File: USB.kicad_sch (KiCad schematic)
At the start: 14 parts, among them J1 USB_B_Micro, Q1 BC847, Q2 BC847, U2 CP2102N-Axx-xQFN28

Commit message: Fixed PCB errors
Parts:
- removed Q2: BC847, Package_TO_SOT_SMD:SOT-363_SC-70-6, symbol Transistor_BJT:BC847
- added Q3: BC847, Package_TO_SOT_SMD:SOT-23, symbol Transistor_BJT:BC847
- Q1: footprint Package_TO_SOT_SMD:SOT-363_SC-70-6 -> Package_TO_SOT_SMD:SOT-23
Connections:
- net DTR: now also Q3.2 (E)
- net IO0: now also Q3.3 (C)
- net at R6.2: now also Q3.1 (B)
- no-connect marks 1 -> 17
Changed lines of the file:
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@@
+	)
+	(no_connect
+		(at 106.68 140.97)
+	)
+	(no_connect
+		(at 106.68 179.07)
+	)
+	(no_connect
+		(at 106.68 158.75)
+	)
+	(no_connect
+		(at 106.68 166.37)
+	)
+	(no_connect
+		(at 106.68 168.91)
+	)
+	(no_connect
+		(at 106.68 176.53)
+	)
+	(no_connect
+		(at 106.68 135.89)
+	)
+	(no_connect
+		(at 106.68 181.61)
+	)
+	(no_connect
+		(at 106.68 163.83)
 	)
 	(no_connect
 		(at 64.77 55.88)
+	)
+	(no_connect
+		(at 106.68 151.13)
+	)
+	(no_connect
+		(at 106.68 148.59)
+	)
+	(no_connect
+		(at 106.68 133.35)
+	)
+	(no_connect
+		(at 106.68 143.51)
+	)
+	(no_connect
+		(at 106.68 161.29)
+	)
+	(no_connect
+		(at 106.68 171.45)
+	)
+	(no_connect
+		(at 106.68 156.21)
 	)
 	(wire
@@
 	(symbol
 		(lib_id "Transistor_BJT:BC847")
-		(at 219.71 44.45 0)
+		(at 219.71 62.23 0)
 		(unit 1)
 		(exclude_from_sim no)
@@
 		(dnp no)
 		(fields_autoplaced yes)
-		(property "Reference" "Q1"
-			(at 224.79 43.1799 0)
+		(property "Reference" "Q3"
+			(at 224.79 60.9599 0)
 			(effects
 				(font
@@
 		)
 		(property "Value" "BC847"
-			(at 224.79 45.7199 0)
+			(at 224.79 63.4999 0)
 			(effects
 				(font
@@
 			)
 		)
-		(property "Footprint" "Package_TO_SOT_SMD:SOT-363_SC-70-6"
-			(at 224.79 46.355 0)
+		(property "Footprint" "Package_TO_SOT_SMD:SOT-23"
+			(at 224.79 64.135 0)
 			(effects
 				(font
@@
 		)
 		(property "Datasheet" "http://www.infineon.com/dgdl/Infineon-BC847SERIES_BC848SERIES_BC849SERIES_BC850SERIES-DS-v01_01-en.pdf?fileId=db3a304314dca389011541d4630a1657"
-			(at 219.71 44.45 0)
+			(at 219.71 62.23 0)
 			(effects
 				(font
@@
 		)
 		(property "Description" "0.1A Ic, 45V Vce, NPN Transistor, SOT-23"
-			(at 219.71 44.45 0)
+			(at 219.71 62.23 0)
 			(effects
 				(font
@@
 		(pin "2"
 		)
+		(pin "1"
+		)
 		(pin "3"
-		)
-		(pin "1"
 		)
 		(instances
 			(project ""
 				(path "/32966cbd-337b-4fa7-b66f-bfe62b1c18c3/450de07c-431b-41c3-b4dc-3003fe77996d"
-					(reference "Q1")
+					(reference "Q3")
 					(unit 1)
 				)
@@
 	(symbol
 		(lib_id "Transistor_BJT:BC847")
-		(at 219.71 62.23 0)
+		(at 219.71 44.45 0)
 		(unit 1)
 		(exclude_from_sim no)
@@
 		(dnp no)
 		(fields_autoplaced yes)
-		(property "Reference" "Q2"
-			(at 224.79 60.9599 0)
+		(property "Reference" "Q1"
+			(at 224.79 43.1799 0)
 			(effects
 				(font
@@
 		)
 		(property "Value" "BC847"
-			(at 224.79 63.4999 0)
+			(at 224.79 45.7199 0)
 			(effects
 				(font
@@
 			)
 		)
-		(property "Footprint" "Package_TO_SOT_SMD:SOT-363_SC-70-6"
-			(at 224.79 64.135 0)
+		(property "Footprint" "Package_TO_SOT_SMD:SOT-23"
+			(at 224.79 46.355 0)
 			(effects
 				(font
@@
 		)
 		(property "Datasheet" "http://www.infineon.com/dgdl/Infineon-BC847SERIES_BC848SERIES_BC849SERIES_BC850SERIES-DS-v01_01-en.pdf?fileId=db3a304314dca389011541d4630a1657"
-			(at 219.71 62.23 0)
+			(at 219.71 44.45 0)
 			(effects
 				(font
@@
 		)
 		(property "Description" "0.1A Ic, 45V Vce, NPN Transistor, SOT-23"
-			(at 219.71 62.23 0)
+			(at 219.71 44.45 0)
 			(effects
 				(font
@@
 		(pin "2"
 		)
+		(pin "1"
+		)
 		(pin "3"
-		)
-		(pin "1"
 		)
 		(instances
 			(project "Airboat"
 				(path "/32966cbd-337b-4fa7-b66f-bfe62b1c18c3/450de07c-431b-41c3-b4dc-3003fe77996d"
-					(reference "Q2")
+					(reference "Q1")
 					(unit 1)
 				)

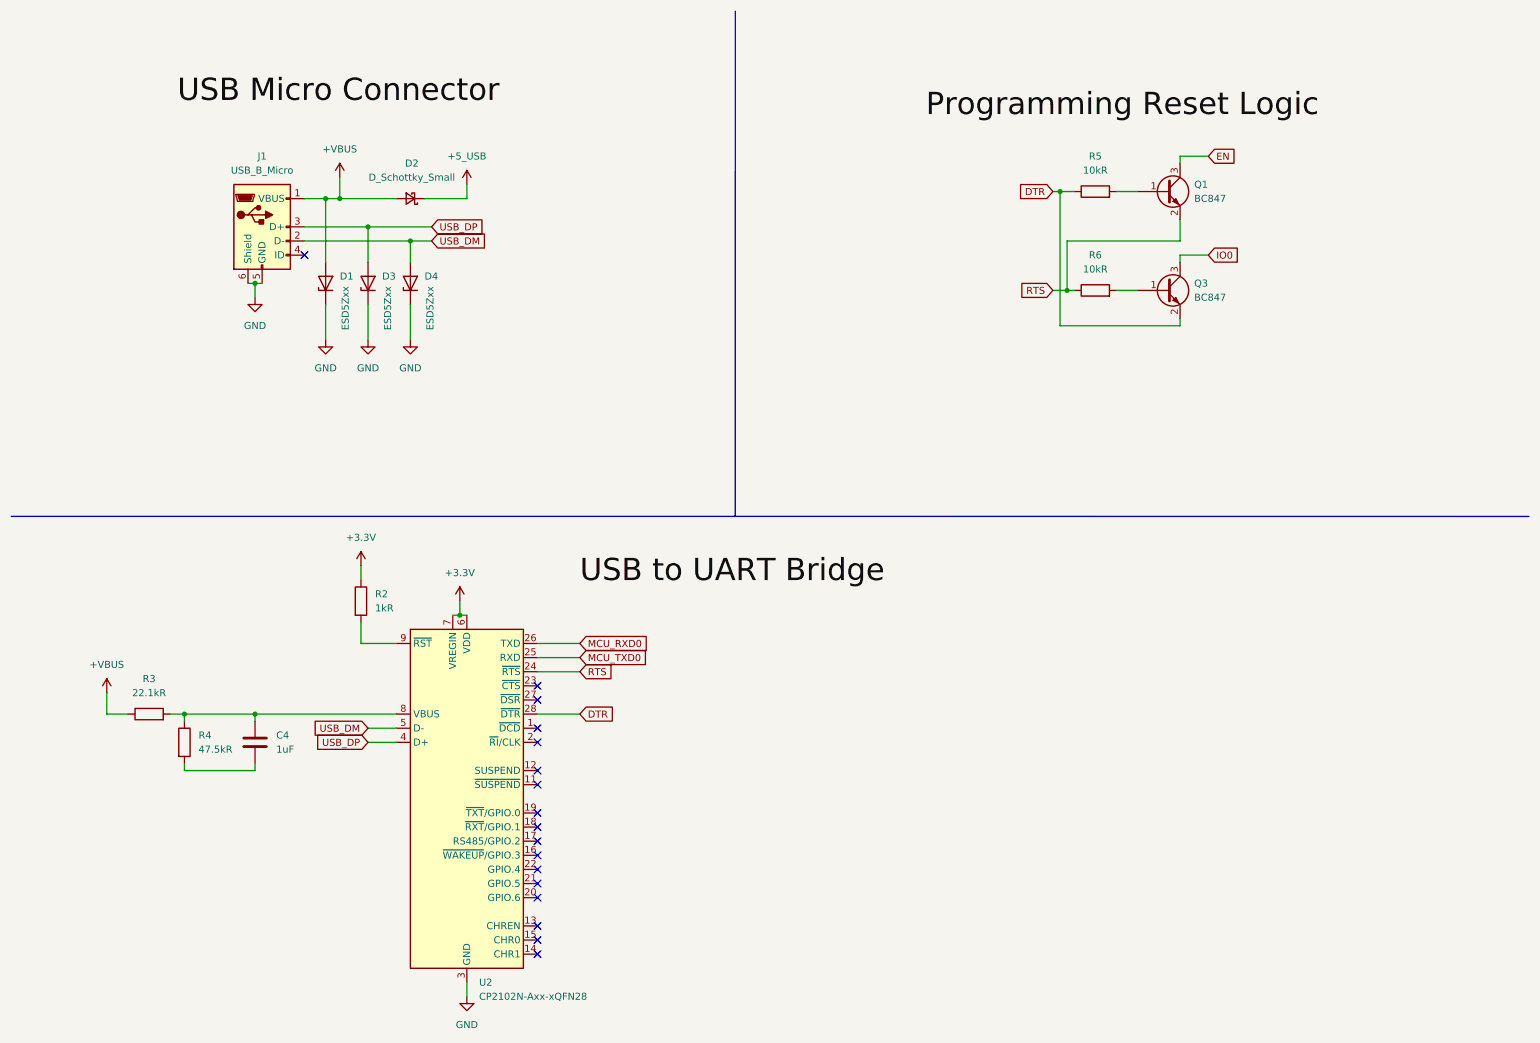
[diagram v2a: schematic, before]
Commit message: Placed all components on PCB
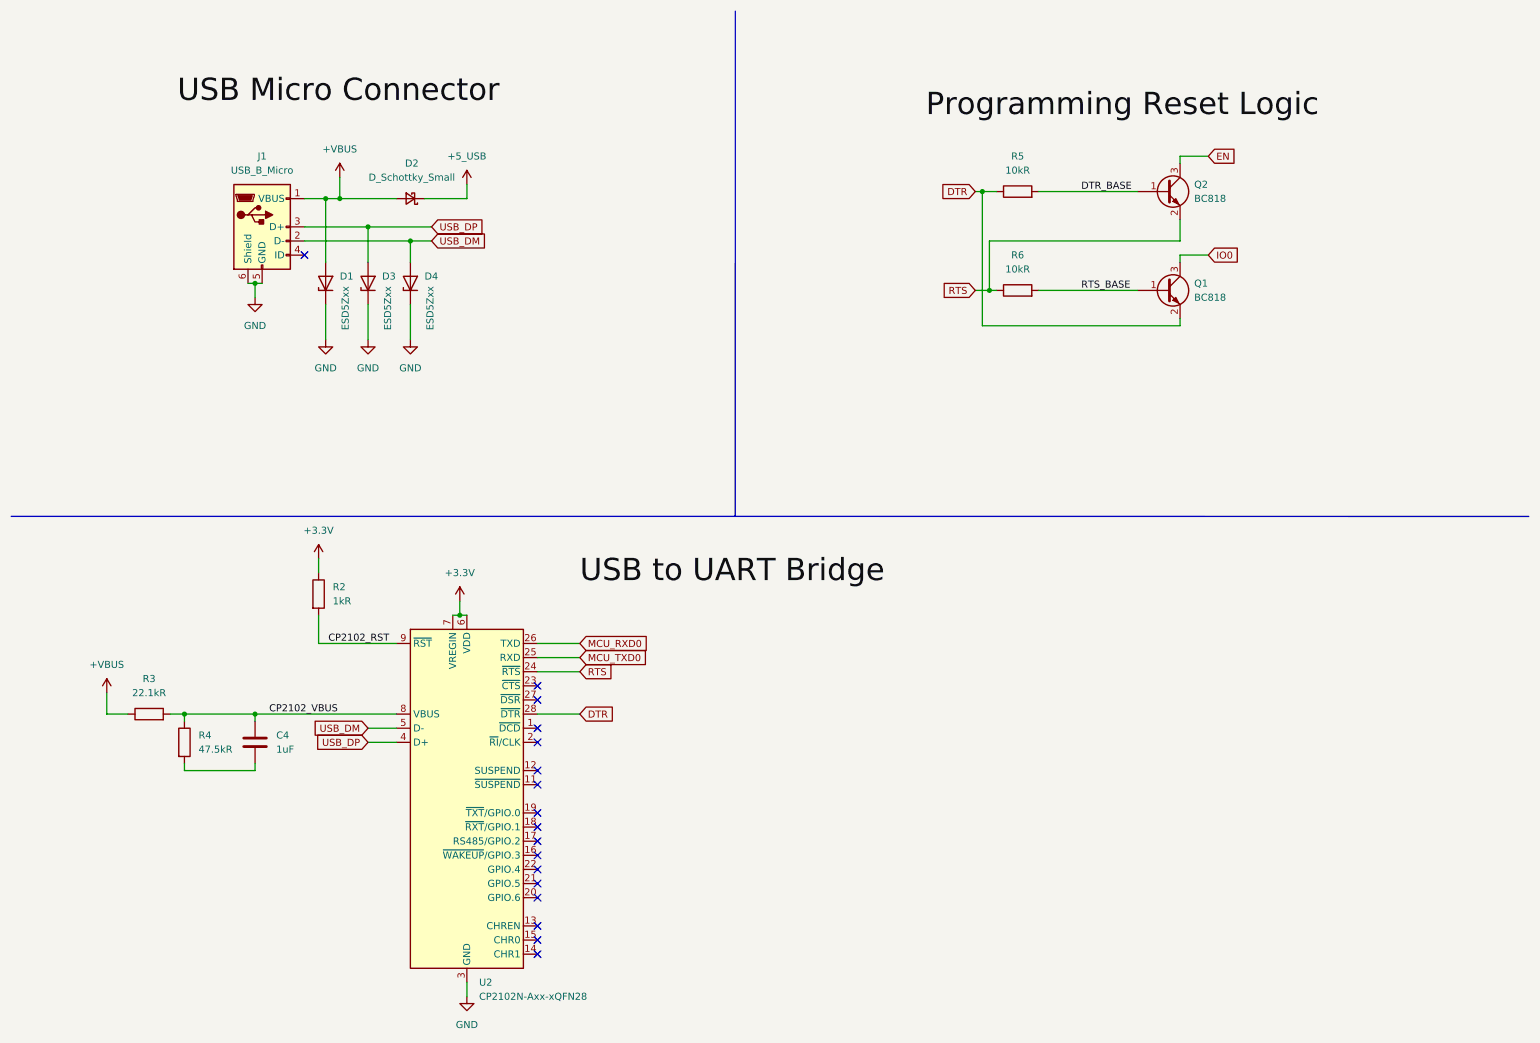
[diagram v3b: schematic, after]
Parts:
- removed Q1, Q3: BC847, Package_TO_SOT_SMD:SOT-23, symbol Transistor_BJT:BC847
- added Q1, Q2: BC818, Package_TO_SOT_SMD:SOT-23, symbol Transistor_BJT:BC818
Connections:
- net DTR: now also Q1.2 (E)
- net EN: now also Q2.3 (C)
- net IO0: now also Q1.3 (C)
- net RTS: now also Q2.2 (E)
- net CP2102_VBUS: now reaches C4.1, R3.2, R4.1, U2.8 (VBUS)
- net CP2102_RST: now reaches R2.2, U2.9 (~{RST})
- net RTS_BASE: now reaches R6.2
- net RTS_BASE: now also Q1.1 (B)
- net DTR_BASE: now reaches R5.2
- net DTR_BASE: now also Q2.1 (B)
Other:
- moved on the sheet: R2, R5, R6

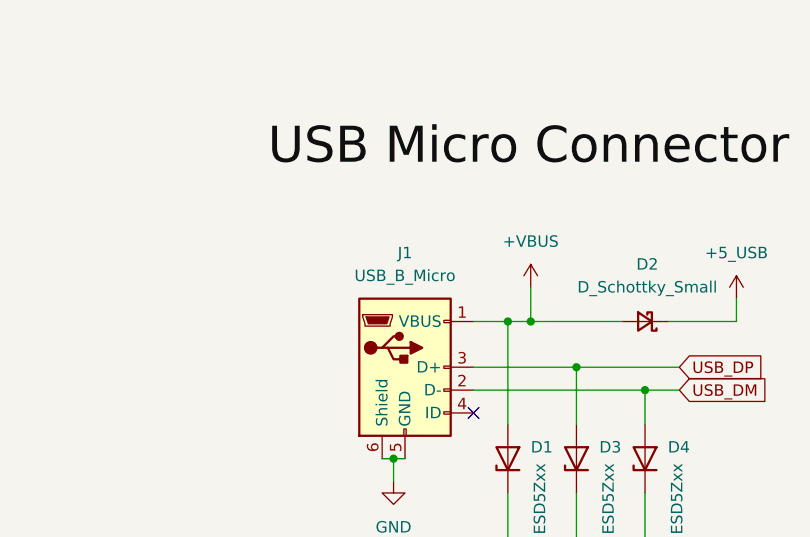
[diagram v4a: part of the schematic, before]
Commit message: Updated PCB to be smaller and support stepper
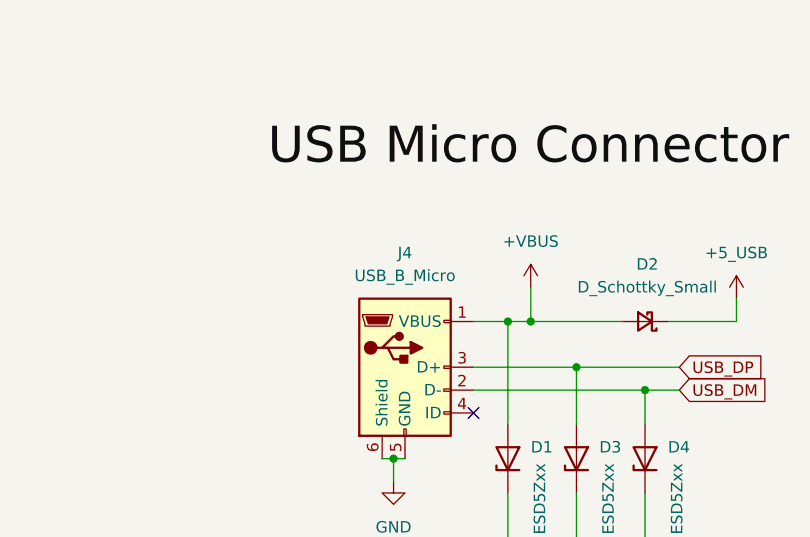
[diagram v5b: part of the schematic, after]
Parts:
- removed J1: USB_B_Micro, Connector_USB:USB_Micro-AB_Molex_47590-0001, symbol Connector:USB_B_Micro
- added J4: USB_B_Micro, Connector_USB:USB_Micro-B_GCT_USB3076-30-A, symbol Connector:USB_B_Micro
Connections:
- net +VBUS: now also J4.1 (VBUS)
- net GND: now also J4.5 (GND), J4.6 (Shield)
- net USB_DM: now also J4.2 (D-)
- net USB_DP: now also J4.3 (D+)
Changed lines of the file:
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@@
-	)
-	(symbol
-		(lib_id "Connector:USB_B_Micro")
-		(at 57.15 50.8 0)
-		(unit 1)
-		(exclude_from_sim no)
-		(in_bom yes)
-		(on_board yes)
-		(dnp no)
-		(fields_autoplaced yes)
-		(property "Reference" "J1"
-			(at 57.15 38.1 0)
-			(effects
-				(font
-					(size 1.27 1.27)
-				)
-			)
-		)
-		(property "Value" "USB_B_Micro"
-			(at 57.15 40.64 0)
-			(effects
-				(font
-					(size 1.27 1.27)
-				)
-			)
-		)
-		(property "Footprint" "Connector_USB:USB_Micro-AB_Molex_47590-0001"
-			(at 60.96 52.07 0)
-			(effects
-				(font
-					(size 1.27 1.27)
-				)
-				(hide yes)
-			)
-		)
-		(property "Datasheet" "~"
-			(at 60.96 52.07 0)
-			(effects
-				(font
-					(size 1.27 1.27)
-				)
-				(hide yes)
-			)
-		)
-		(property "Description" "USB Micro Type B connector"
-			(at 57.15 50.8 0)
-			(effects
-				(font
-					(size 1.27 1.27)
-				)
-				(hide yes)
-			)
-		)
-		(pin "6"
-		)
-		(pin "2"
-		)
-		(pin "1"
-		)
-		(pin "4"
-		)
-		(pin "5"
-		)
-		(pin "3"
-		)
-		(instances
-			(project "Airboat"
-				(path "/32966cbd-337b-4fa7-b66f-bfe62b1c18c3/450de07c-431b-41c3-b4dc-3003fe77996d"
-					(reference "J1")
-					(unit 1)
-				)
-			)
-		)
 	)
 	(symbol
@@
 					(unit 1)
 				)
+			)
+		)
+	)
+	(symbol
+		(lib_id "Connector:USB_B_Micro")
+		(at 57.15 50.8 0)
+		(unit 1)
+		(exclude_from_sim no)
+		(in_bom yes)
+		(on_board yes)
+		(dnp no)
+		(fields_autoplaced yes)
+		(property "Reference" "J4"
+			(at 57.15 38.1 0)
+			(effects
+				(font
+					(size 1.27 1.27)
+				)
+			)
+		)
+		(property "Value" "USB_B_Micro"
+			(at 57.15 40.64 0)
+			(effects
+				(font
+					(size 1.27 1.27)
+				)
+			)
+		)
+		(property "Footprint" "Connector_USB:USB_Micro-B_GCT_USB3076-30-A"
+			(at 60.96 52.07 0)
+			(effects
+				(font
+					(size 1.27 1.27)
+				)
+				(hide yes)
+			)
+		)
+		(property "Datasheet" "~"
+			(at 60.96 52.07 0)
+			(effects
+				(font
+					(size 1.27 1.27)
+				)
+				(hide yes)
+			)
+		)
+		(property "Description" "USB Micro Type B connector"
+			(at 57.15 50.8 0)
+			(effects
+				(font
+					(size 1.27 1.27)
+				)
+				(hide yes)
+			)
+		)
+		(pin "1"
+		)
+		(pin "2"
+		)
+		(pin "5"
+		)
+		(pin "4"
+		)
+		(pin "3"
+		)
+		(pin "6"
+		)
+		(instances
+			(project ""
+				(path "/32966cbd-337b-4fa7-b66f-bfe62b1c18c3/450de07c-431b-41c3-b4dc-3003fe77996d"
+					(reference "J4")
+					(unit 1)
+				)

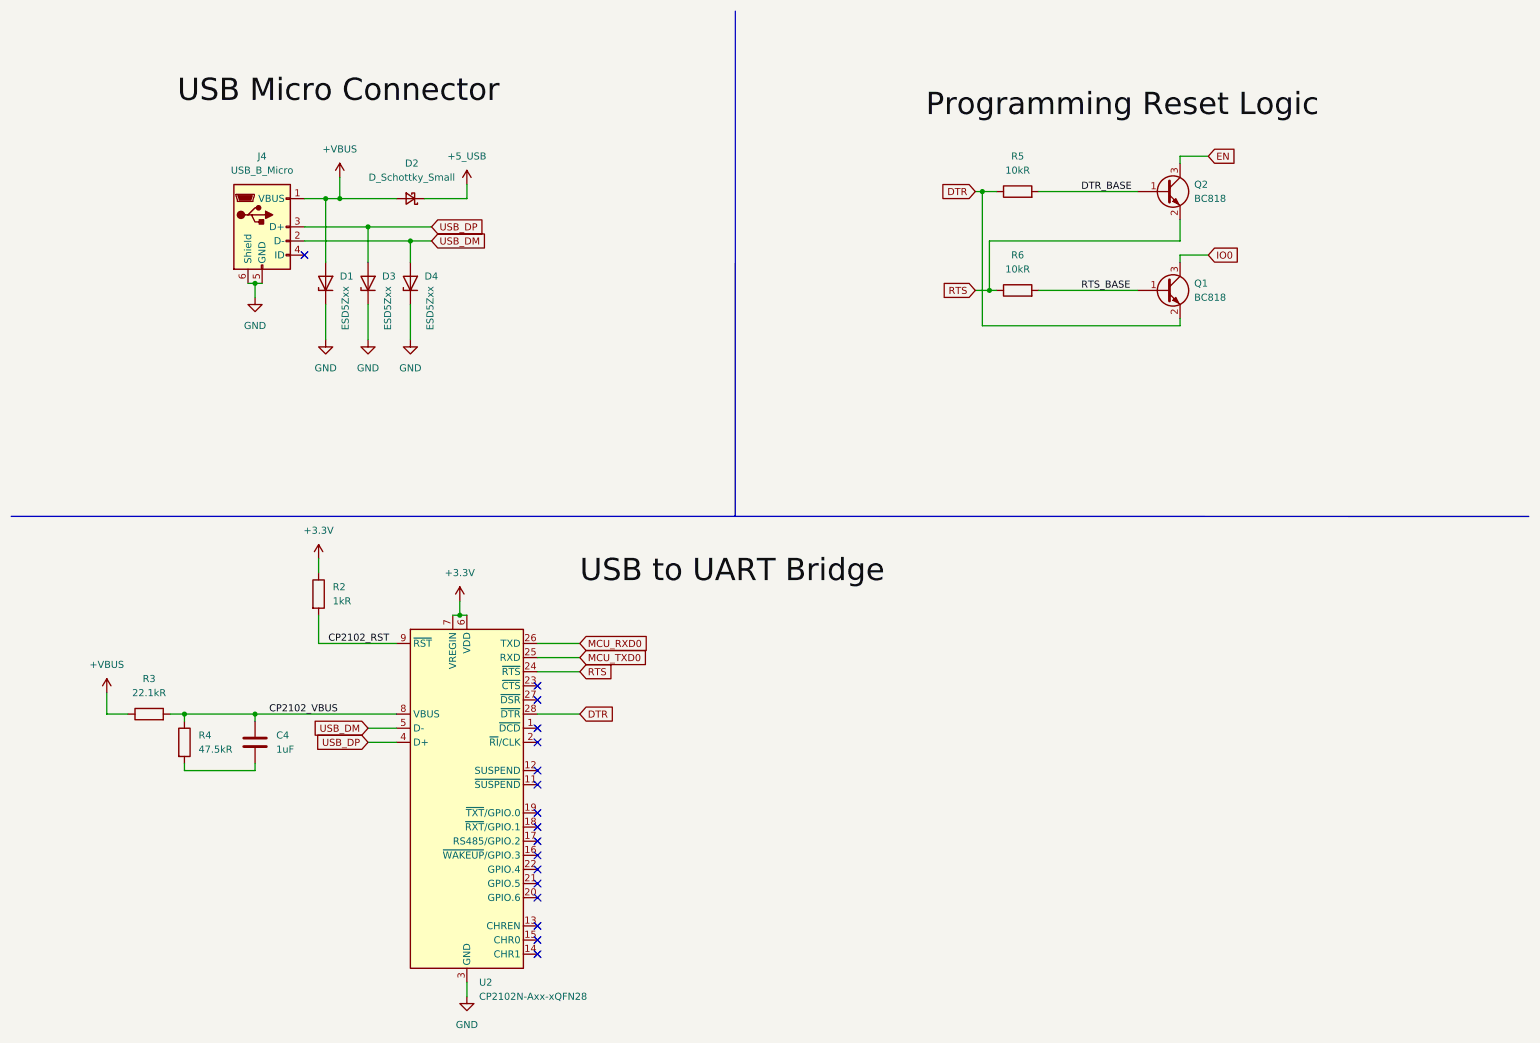
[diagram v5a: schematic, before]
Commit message: Updated to use boost converters
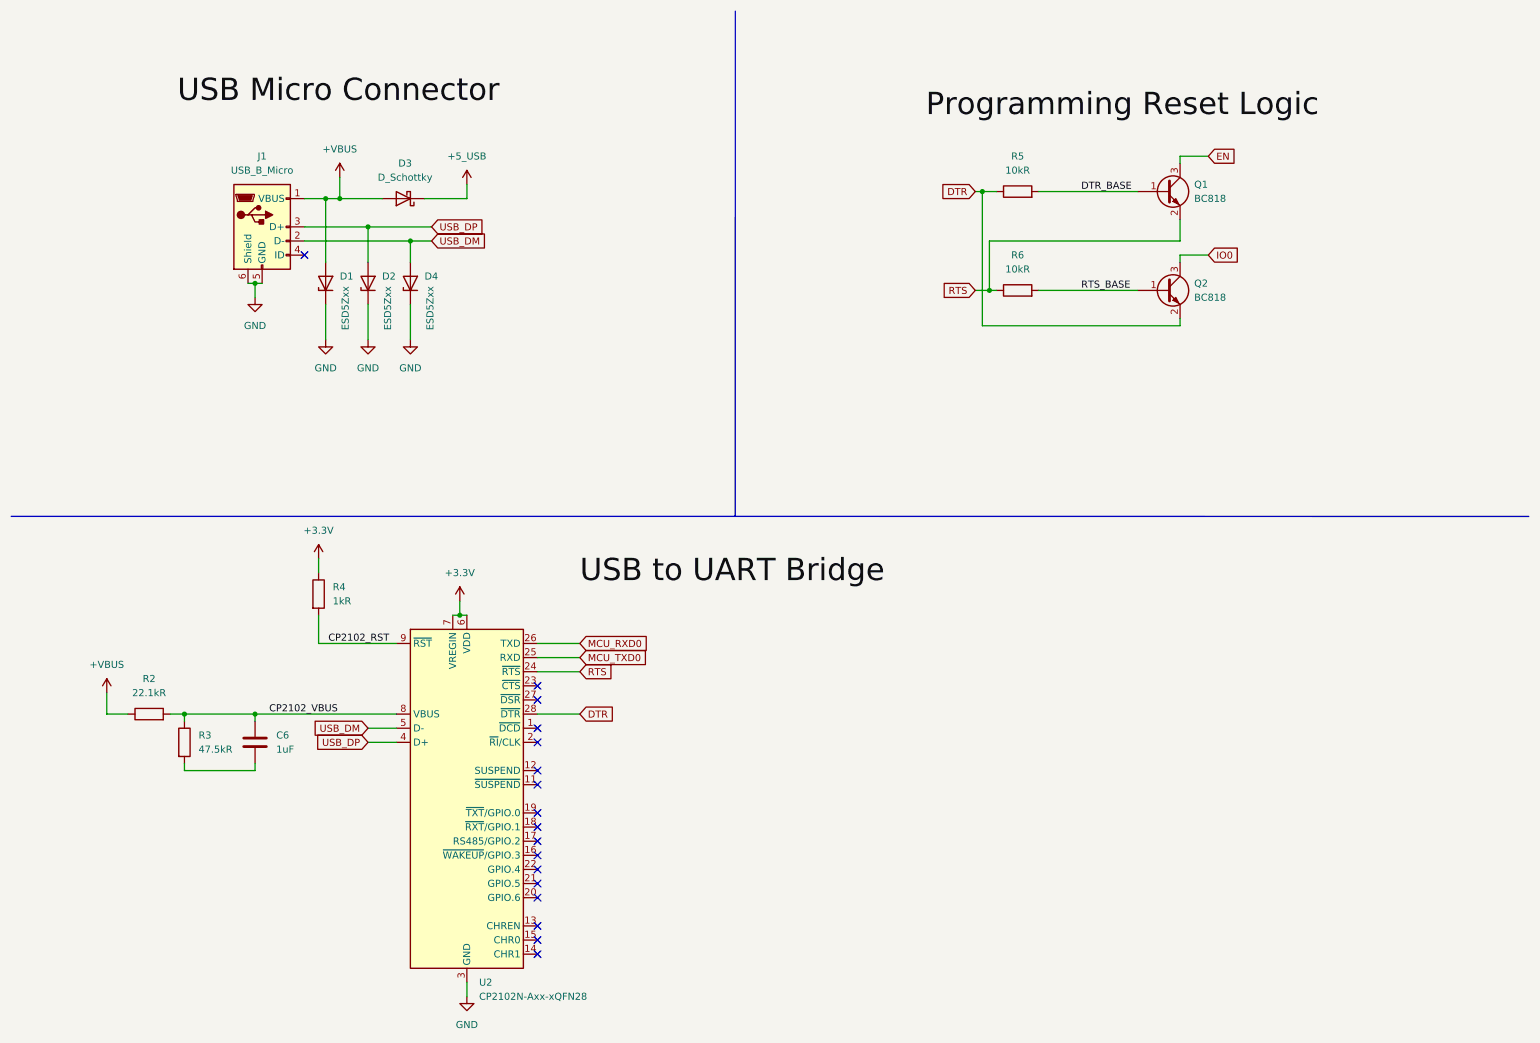
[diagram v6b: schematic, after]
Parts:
- removed D2: D_Schottky_Small, Diode_SMD:D_SOD-523, symbol Device:D_Schottky_Small
- added D3: D_Schottky, Diode_SMD:D_SMC, symbol Device:D_Schottky
- renumbered C4 to C6, D3 to D2, J4 to J1, Q2 to Q1, Q1 to Q2, R3 to R2, R4 to R3, R2 to R4
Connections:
- net +5_USB: now also D3.1 (K)
- net +VBUS: now also D3.2 (A)
